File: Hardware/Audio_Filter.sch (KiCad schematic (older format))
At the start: 26 parts, among them U3 NE5534, U4 NE5534, U5 NE5534

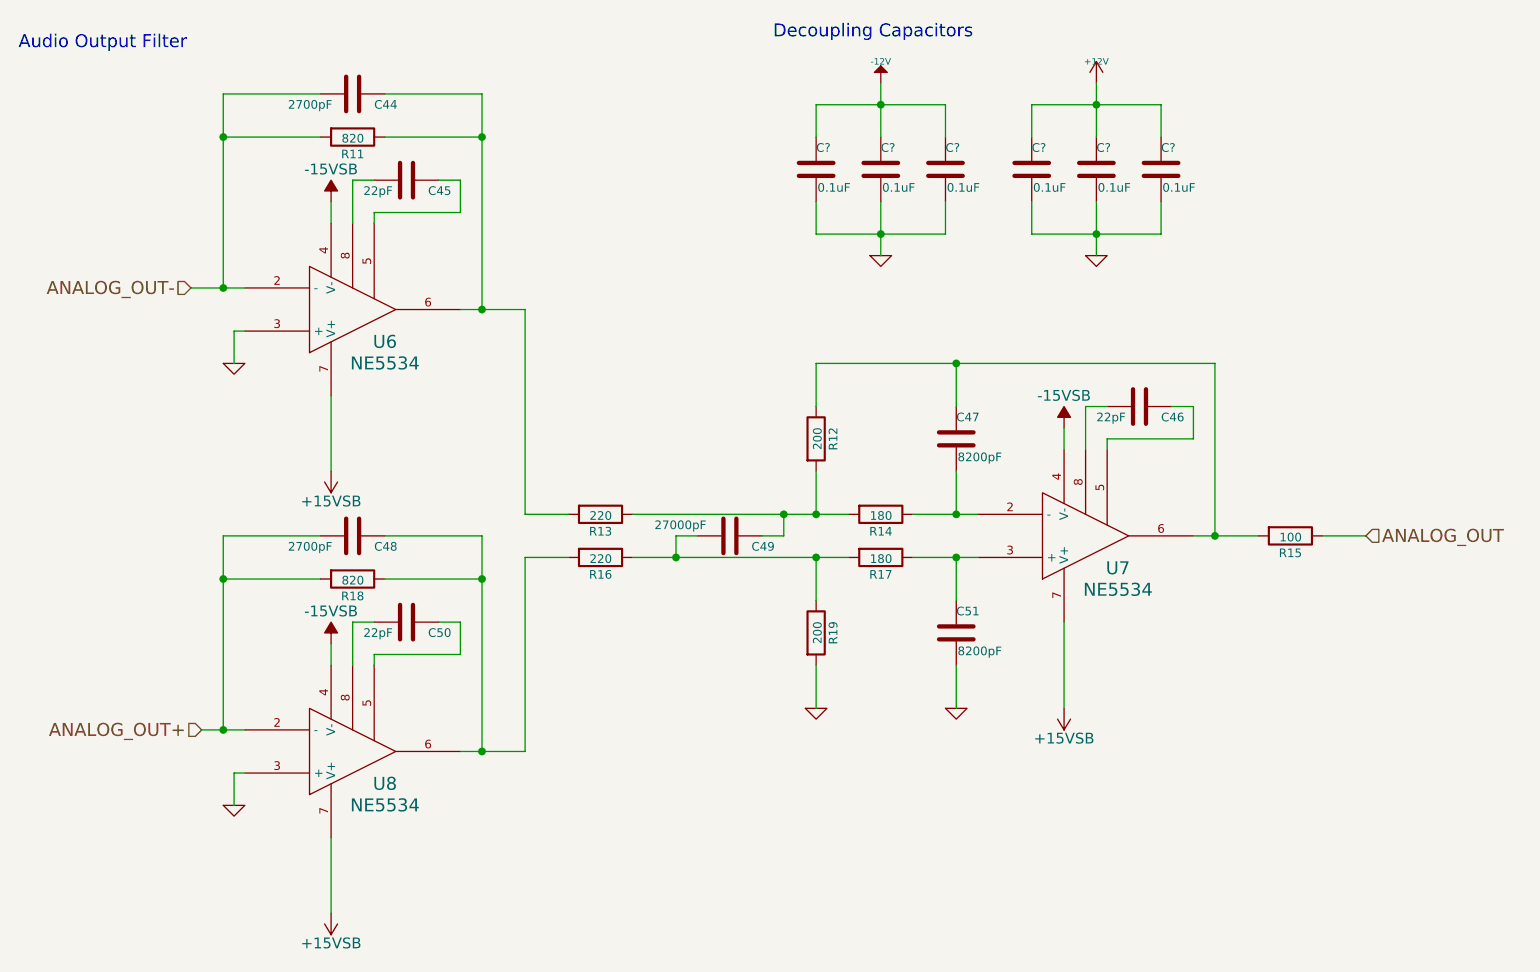
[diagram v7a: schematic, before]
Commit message: Made design review fixes, added breakouts
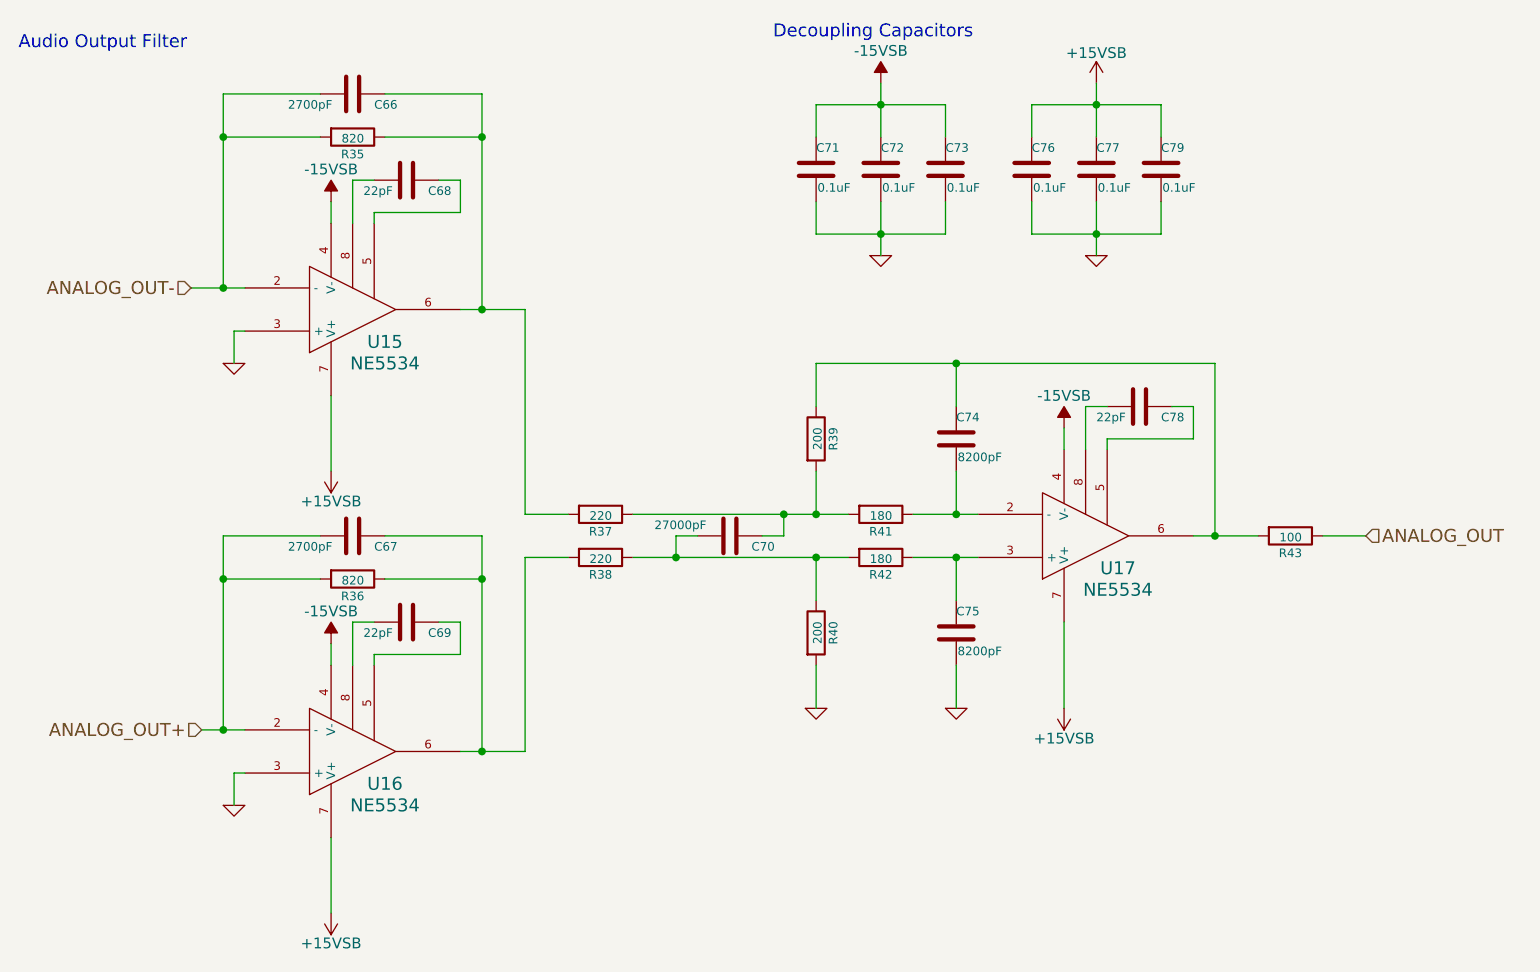
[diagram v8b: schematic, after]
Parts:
- gave numbers to parts that had none: 6
- renumbered C36 to C52, C40 to C53, C37 to C54, C42 to C55, C41 to C56, C39 to C60, C43 to C61, C38 to C64, R2 to R26, R9 to R27, R4 to R28, R7 to R29, R3 to R30, R10 to R31, R5 to R32, R8 to R33, R6 to R34, U3 to U12, U5 to U13, U4 to U14
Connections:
- net +12V is gone; now on net +15V: C62.1, C63.1, C65.1
- net -12V is gone; now on net -15V: C57.1, C58.1, C59.1
